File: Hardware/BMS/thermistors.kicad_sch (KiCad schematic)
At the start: 6 parts, among them U2 MAX14661ETI+T, U6 MAX14661ETI+T

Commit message: edits to the BMS
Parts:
- removed R51, R52, R67, R68: 3.3k, symbol Device:R
- removed U2, U6: MAX14661ETI+T, 21-0139I_T2844-1_MXM, symbol MAX14661:MAX14661ETI+T
- added C301, C302, C303, C304, C306, C308: 1uF, Capacitor_SMD:C_0603_1608Metric, symbol Device:C
- added C305, C307: 0.1uF, Capacitor_SMD:C_0603_1608Metric, symbol Device:C
- added J301, J302: Conn_02x09_Counter_Clockwise, Connector_PinSocket_2.54mm:PinSocket_2x09_P2.54mm_Vertical, symbol Connector_Generic:Conn_02x09_Counter_Clockwise
- added R301, R302, R303, R304, R305, R306, R307, R308, R309, R310, R311, R312, R313, R314, R315, R316, R317, R318, R319, R320, R321, R322, R323, R324, R325, R326, R327, R328, R329, R330: 100k, symbol Device:R
- added R335, R336: 3.3k, symbol Device:R
- added TH101: Thermistor, Resistor_SMD:R_0603_1608Metric, symbol Device:Thermistor
- added U301, U303: MAX14661ETI+T, BAD_LIB:21-0139I_T2844-1_MXM, symbol OlinBAD:MAX14661ETI+T
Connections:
- net GND: now also C301.2, C302.2, C303.2, C304.2, C305.2, C306.2, C307.2, C308.2, J301.14 (Pin_14), J301.9 (Pin_9), J302.1 (Pin_1), J302.14 (Pin_14), J302.2 (Pin_2), J302.3 (Pin_3), J302.4 (Pin_4), J302.9 (Pin_9), TH101.2, U301.1 (*SPI/I2C), U301.11 (GND), U301.23 (*CS/A0), U301.25 (GND), U301.29 (EPAD), U303.1 (*SPI/I2C), U303.11 (GND), U303.23 (*CS/A0), U303.25 (GND), U303.28 (DOUT/A1), U303.29 (EPAD)
- net THERM_A1: now also U303.10 (COMA)
- net THERM_A2: now also U301.10 (COMA)
- net THERM_B1: now also U303.13 (COMB)
- net THERM_B2: now also U301.13 (COMB)
- new net: TH101.1, U301.16 (AB14)
- new net +3.3V: C301.1, C302.1, C303.1, C304.1, C305.1, C306.1, C307.1, C308.1, R301.2, R302.2, R303.2, R304.2, R305.2, R306.2, R307.2, R308.2, R309.2, R310.2, R311.2, R312.2, R313.2, R314.2, R315.2, R316.2, R317.2, R318.2, R319.2, R320.2, R321.2, R322.2, R323.2, R324.2, R325.2, R326.2, R327.2, R328.2, R329.2, R330.2, R335.1, R336.1, U301.22 (*SD), U301.26 (VCC), U301.28 (DOUT/A1), U303.22 (*SD), U303.26 (VCC)
- new net SCL: R336.2, U301.24 (SCLK/SCL), U303.24 (SCLK/SCL)
- new net SDA: R335.2, U301.27 (DIN/SDA), U303.27 (DIN/SDA)
- new net THERM_AMBIENT: R330.1
- new net THERM_BUSBAR: R323.1, U301.17 (AB13)
- new net TH_1_A: J301.18 (Pin_18), R301.1, U303.2 (AB01)
- new net TH_1_B: J301.17 (Pin_17), R309.1, U303.3 (AB02)
- new net TH_1_C: J301.16 (Pin_16), R302.1, U303.4 (AB03)
- new net TH_1_D: J301.15 (Pin_15), R310.1, U303.5 (AB04)
- new net TH_2_A: J301.13 (Pin_13), R303.1, U303.6 (AB05)
- new net TH_2_B: J301.12 (Pin_12), R311.1, U303.7 (AB06)
- new net TH_2_C: J301.11 (Pin_11), R304.1, U303.8 (AB07)
- new net TH_2_D: J301.10 (Pin_10), R312.1, U303.9 (AB08)
- new net TH_3_A: J301.7 (Pin_7), R306.1, U303.19 (AB11)
- new net TH_3_B: J301.8 (Pin_8), R314.1, U303.18 (AB12)
- new net TH_3_C: J301.5 (Pin_5), R305.1, U303.21 (AB09)
- new net TH_3_D: J301.6 (Pin_6), R313.1, U303.20 (AB10)
- new net TH_4_A: J301.3 (Pin_3), R307.1, U303.17 (AB13)
- new net TH_4_B: J301.4 (Pin_4), R315.1, U303.16 (AB14)
- new net TH_4_C: J301.1 (Pin_1), R308.1, U303.15 (AB15)
- new net TH_4_D: J301.2 (Pin_2), R316.1, U303.14 (AB16)
- new net TH_5_A: J302.18 (Pin_18), R317.1, U301.2 (AB01)
- new net TH_5_B: J302.17 (Pin_17), R324.1, U301.3 (AB02)
- new net TH_5_C: J302.16 (Pin_16), R318.1, U301.4 (AB03)
- new net TH_5_D: J302.15 (Pin_15), R325.1, U301.5 (AB04)
- new net TH_6_A: J302.13 (Pin_13), R319.1, U301.6 (AB05)
- new net TH_6_B: J302.12 (Pin_12), R326.1, U301.7 (AB06)
- new net TH_6_C: J302.11 (Pin_11), R320.1, U301.8 (AB07)
- new net TH_6_D: J302.10 (Pin_10), R327.1, U301.9 (AB08)
- new net TH_7_A: J302.8 (Pin_8), R321.1, U301.18 (AB12)
- new net TH_7_B: J302.7 (Pin_7), R328.1, U301.19 (AB11)
- new net TH_7_C: J302.6 (Pin_6), R322.1, U301.20 (AB10)
- new net TH_7_D: J302.5 (Pin_5), R329.1, U301.21 (AB09)
- no-connect marks 4 -> 2
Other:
- removed sheet Cell Thermistor1
- removed sheet Cell Thermistor10
- removed sheet Cell Thermistor11
- removed sheet Cell Thermistor12
- removed sheet Cell Thermistor13
- removed sheet Cell Thermistor14
- removed sheet Cell Thermistor15
- removed sheet Cell Thermistor16
- removed sheet Cell Thermistor17
- removed sheet Cell Thermistor18
- removed sheet Cell Thermistor19
- removed sheet Cell Thermistor2
- removed sheet Cell Thermistor20
- removed sheet Cell Thermistor21
- removed sheet Cell Thermistor22
- removed sheet Cell Thermistor23
- removed sheet Cell Thermistor24
- removed sheet Cell Thermistor25
- removed sheet Cell Thermistor26
- removed sheet Cell Thermistor27
- removed sheet Cell Thermistor28
- removed sheet Cell Thermistor3
- removed sheet Cell Thermistor4
- removed sheet Cell Thermistor5
- removed sheet Cell Thermistor6
- removed sheet Cell Thermistor7
- removed sheet Cell Thermistor8
- removed sheet Cell Thermistor9
- note added: "Ambient thermistor for reference"

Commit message: updated some stm stuff and added current sense amplifier for main pack
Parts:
- R301, R302, R303, R304, R305, R306, R307, R308, R309, R310, R311, R312, R313, R314, R315, R316, R317, R318, R319, R320, R321, R322, R323, R324, R325, R326, R327, R328, R329, R330: footprint (none) -> Resistor_SMD:R_0603_1608Metric

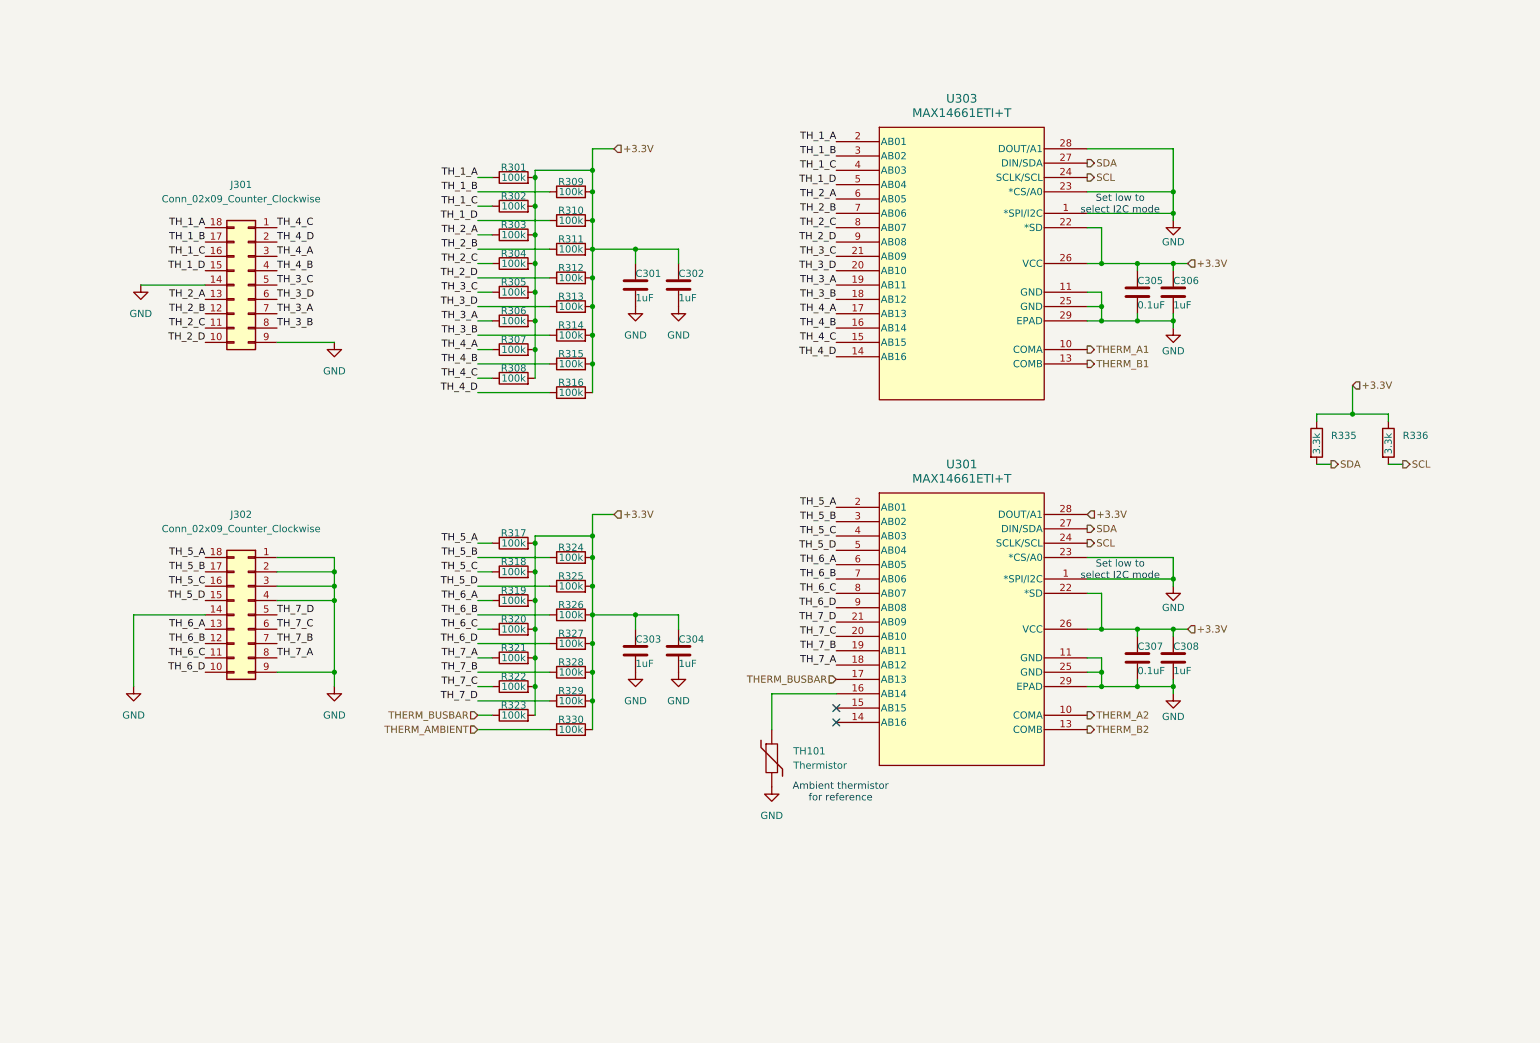
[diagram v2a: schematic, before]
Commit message: Add test points and LEDs
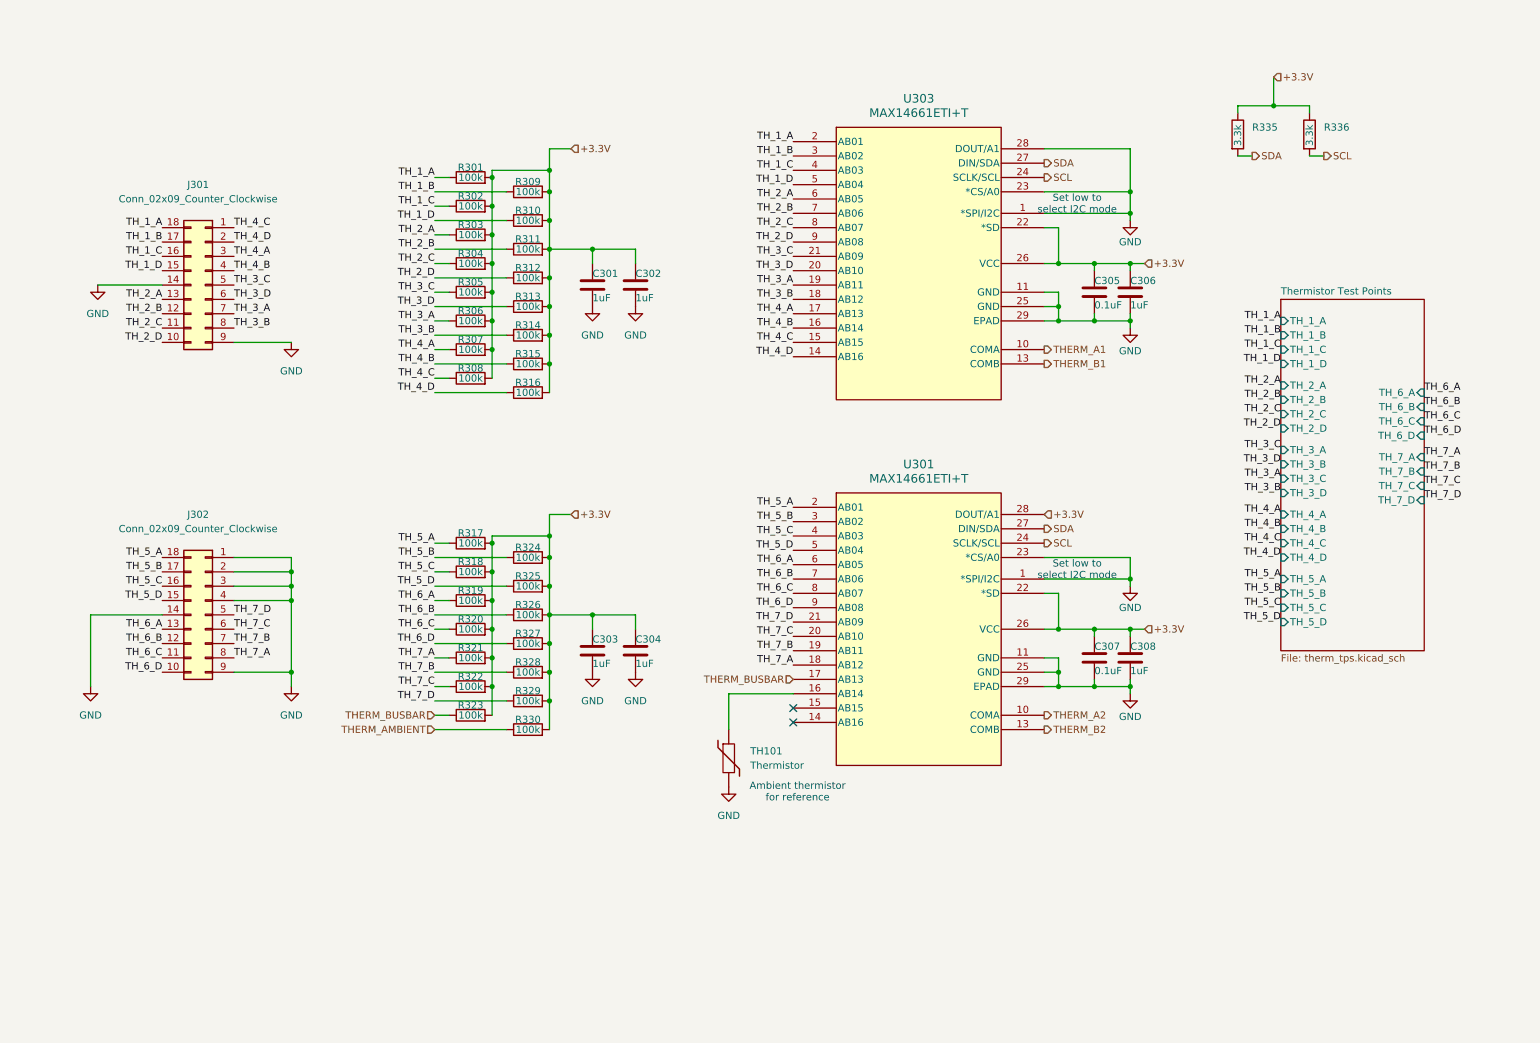
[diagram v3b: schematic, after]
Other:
- added sheet Thermistor Test Points (therm_tps.kicad_sch)
- moved on the sheet: C301, C302, C303, C304, C305, C306, C307, C308, J301, J302, R301, R302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

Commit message: begin layout
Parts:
- removed R335, R336: 3.3k, symbol Device:R
- added R331, R332: 3.3k, Resistor_SMD:R_0603_1608Metric, symbol Device:R
- renumbered C303 to C301, C301 to C302, C304 to C303, C302 to C304, C307 to C306, C306 to C307, R317 to R301, R318 to R302, R319 to R303, R320 to R304, R321 to R305, R322 to R306, R323 to R307, R301 to R308, R302 to R309, R303 to R310, R304 to R311, R305 to R312, R306 to R313, R307 to R314, R308 to R315, R324 to R316, R325 to R317, R326 to R318, R327 to R319, R328 to R320, R329 to R321, R330 to R322, R309 to R323, R310 to R324, R311 to R325, R312 to R326, R313 to R327, R314 to R328, R315 to R329, R316 to R330, TH101 to TH301, U303 to U301, U301 to U302
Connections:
- net +3.3V: now also R331.1, R332.1
- net SCL: now also R332.2
- net SDA: now also R331.2
- net THERM_AMBIENT: now also TH301.1, U302.16 (AB14)
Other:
- moved on the sheet: C301, C303, R301, R302, R303, R304, R305, R306, R307, R316, R317, R318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
